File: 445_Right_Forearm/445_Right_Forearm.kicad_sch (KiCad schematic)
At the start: 2 parts, among them J1 69167-107HLF, U1 LSM6DSMTR

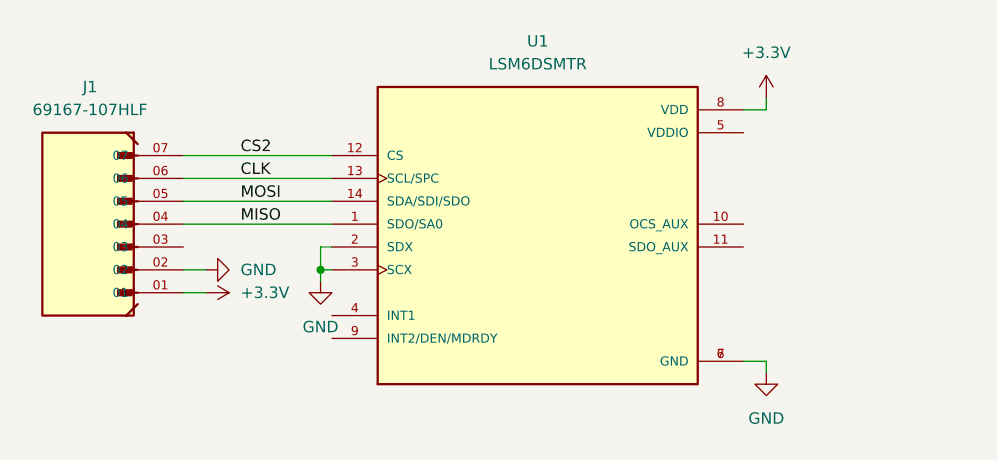
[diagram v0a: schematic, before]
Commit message: enable signal and analog switches
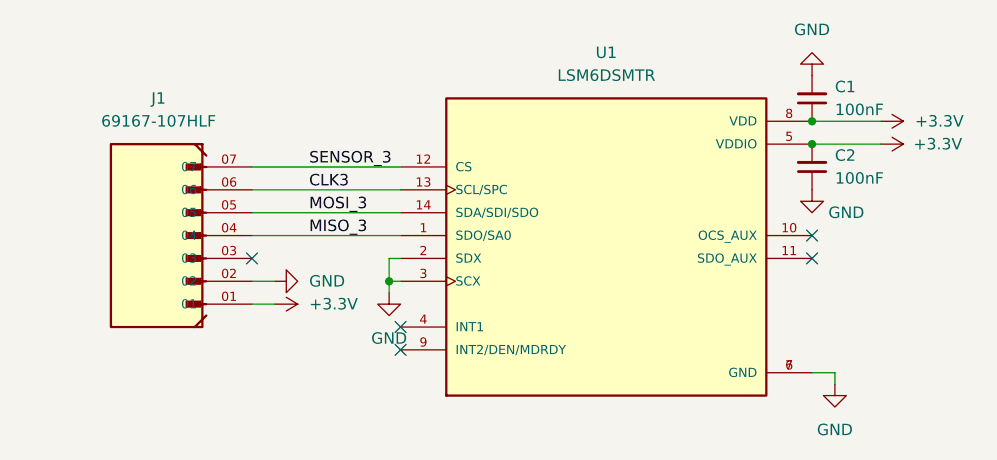
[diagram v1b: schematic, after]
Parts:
- added C1, C2: 100nF, symbol Device:C_Small
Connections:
- net +3.3V: now also U1.5 (VDDIO), C1.1, C2.2
- net GND: now also C1.2, C2.1
- net CLK renamed CLK3
- net CS2 renamed SENSOR_3
- net MISO renamed MISO_3
- net MOSI renamed MOSI_3
- no-connect marks 0 -> 5

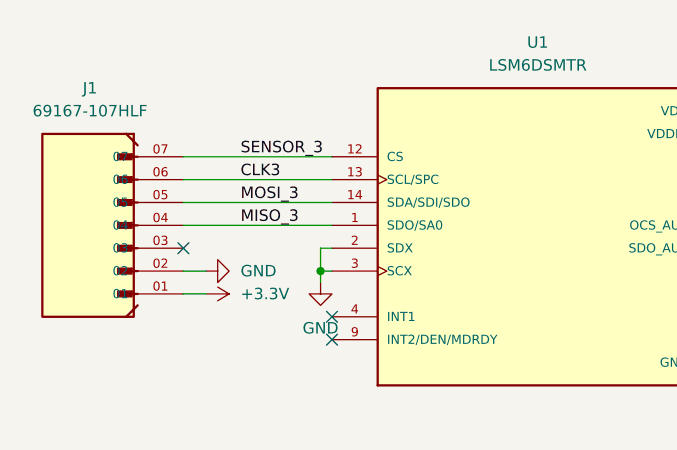
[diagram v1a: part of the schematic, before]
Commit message: replace bicep connector and add int1 connections
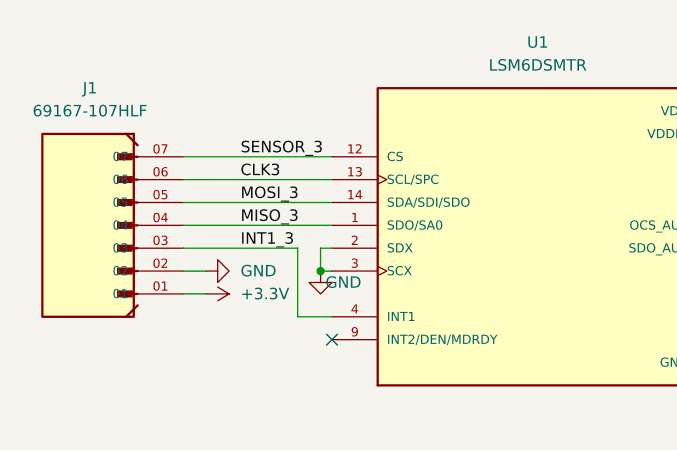
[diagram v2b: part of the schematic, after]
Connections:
- net INT1_3: now reaches J1.03
- net INT1_3: now also U1.4 (INT1)
- no-connect marks 5 -> 3
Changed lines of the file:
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@@
   (junction (at 191.77 77.47) (diameter 0) (color 0 0 0 0)
   )
-  (no_connect (at 146.05 100.33))
   (no_connect (at 191.77 92.71))
-  (no_connect (at 129.54 92.71))
   (no_connect (at 191.77 90.17))
   (no_connect (at 146.05 102.87))
   (wire (pts (xy 191.77 105.41) (xy 194.31 105.41))
-    (stroke (width 0) (type default))
-  )
-  (wire (pts (xy 144.78 95.25) (xy 144.78 92.71))
     (stroke (width 0) (type default))
   )
@@
     (stroke (width 0) (type default))
   )
+  (wire (pts (xy 142.24 92.71) (xy 142.24 100.33))
+    (stroke (width 0) (type default))
+  )
   (wire (pts (xy 194.31 105.41) (xy 194.31 106.68))
     (stroke (width 0) (type default))
@@
     (stroke (width 0) (type default))
   )
-  (wire (pts (xy 144.78 95.25) (xy 146.05 95.25))
+  (wire (pts (xy 129.54 92.71) (xy 142.24 92.71))
     (stroke (width 0) (type default))
   )
-  (wire (pts (xy 144.78 96.52) (xy 144.78 95.25))
+  (wire (pts (xy 144.78 95.25) (xy 146.05 95.25))
     (stroke (width 0) (type default))
   )
@@
     (stroke (width 0) (type default))
   )
+  (wire (pts (xy 144.78 92.71) (xy 144.78 95.25))
+    (stroke (width 0) (type default))
+  )
   (wire (pts (xy 129.54 97.79) (xy 132.08 97.79))
+    (stroke (width 0) (type default))
+  )
+  (wire (pts (xy 142.24 100.33) (xy 146.05 100.33))
     (stroke (width 0) (type default))
   )
@@
   )
   (label "SENSOR_3" (at 135.89 82.55 0) (fields_autoplaced)
+    (effects (font (size 1.27 1.27)) (justify left bottom))
+  )
+  (label "INT1_3" (at 135.89 92.71 0) (fields_autoplaced)
     (effects (font (size 1.27 1.27)) (justify left bottom))
   )
@@
     )
   )
-  (symbol (lib_id "power:GND") (at 144.78 96.52 0) (unit 1)
-    (in_bom yes) (on_board yes) (dnp no) (fields_autoplaced)
-    (property "Reference" "#PWR03" (at 144.78 102.87 0)
+  (symbol (lib_id "power:GND") (at 144.78 95.25 0) (unit 1)
+    (in_bom yes) (on_board yes) (dnp no)
+    (property "Reference" "#PWR03" (at 144.78 101.6 0)
       (effects (font (size 1.27 1.27)) hide)
     )
-    (property "Value" "GND" (at 144.78 101.6 0)
+    (property "Value" "GND" (at 147.32 96.52 0)
       (effects (font (size 1.27 1.27)))
     )
-    (property "Footprint" "" (at 144.78 96.52 0)
+    (property "Footprint" "" (at 144.78 95.25 0)
       (effects (font (size 1.27 1.27)) hide)
     )
-    (property "Datasheet" "" (at 144.78 96.52 0)
+    (property "Datasheet" "" (at 144.78 95.25 0)
       (effects (font (size 1.27 1.27)) hide)
     )

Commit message: Layout First Draft
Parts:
- added H1, H2, H3, H4: MountingHole, MountingHole:MountingHole_2mm, symbol Mechanical:MountingHole
- C1, C2: footprint (none) -> CL21F104ZAANNNC:CAPC2012X135N
- renumbered J1 to J7, U1 to U8
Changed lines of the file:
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@@
     (effects (font (size 1.27 1.27)) (justify left bottom))
+  )
+  (symbol (lib_id "Mechanical:MountingHole") (at 25.4 20.32 0) (unit 1)
+    (in_bom yes) (on_board yes) (dnp no) (fields_autoplaced)
+    (property "Reference" "H1" (at 27.94 19.05 0)
+      (effects (font (size 1.27 1.27)) (justify left))
+    )
+    (property "Value" "MountingHole" (at 27.94 21.59 0)
+      (effects (font (size 1.27 1.27)) (justify left))
+    )
+    (property "Footprint" "MountingHole:MountingHole_2mm" (at 25.4 20.32 0)
+      (effects (font (size 1.27 1.27)) hide)
+    )
+    (property "Datasheet" "~" (at 25.4 20.32 0)
+      (effects (font (size 1.27 1.27)) hide)
+    )
+    (instances
+      (project "445_Right_Forearm"
+        (path "/6bc04bea-814c-4bc3-8d6d-db11891cde88"
+          (reference "H1") (unit 1)
+        )
+      )
+    )
   )
   (symbol (lib_id "power:GND") (at 132.08 95.25 90) (unit 1)
@@
       (effects (font (size 1.27 1.27)) (justify right))
     )
-    (property "Footprint" "" (at 191.77 82.55 0)
+    (property "Footprint" "CL21F104ZAANNNC:CAPC2012X135N" (at 191.77 82.55 0)
       (effects (font (size 1.27 1.27)) hide)
     )
@@
   (symbol (lib_id "69167-107HLF:69167-107HLF") (at 119.38 90.17 180) (unit 1)
     (in_bom yes) (on_board yes) (dnp no) (fields_autoplaced)
-    (property "Reference" "J1" (at 119.1635 74.93 0)
+    (property "Reference" "J7" (at 119.1635 74.93 0)
       (effects (font (size 1.27 1.27)))
     )
@@
       (project "445_Right_Forearm"
         (path "/6bc04bea-814c-4bc3-8d6d-db11891cde88"
-          (reference "J1") (unit 1)
+          (reference "J7") (unit 1)
+        )
+      )
+    )
+  )
+  (symbol (lib_id "Mechanical:MountingHole") (at 25.4 46.99 0) (unit 1)
+    (in_bom yes) (on_board yes) (dnp no) (fields_autoplaced)
+    (property "Reference" "H4" (at 27.94 45.72 0)
+      (effects (font (size 1.27 1.27)) (justify left))
+    )
+    (property "Value" "MountingHole" (at 27.94 48.26 0)
+      (effects (font (size 1.27 1.27)) (justify left))
+    )
+    (property "Footprint" "MountingHole:MountingHole_2mm" (at 25.4 46.99 0)
+      (effects (font (size 1.27 1.27)) hide)
+    )
+    (property "Datasheet" "~" (at 25.4 46.99 0)
+      (effects (font (size 1.27 1.27)) hide)
+    )
+    (instances
+      (project "445_Right_Forearm"
+        (path "/6bc04bea-814c-4bc3-8d6d-db11891cde88"
+          (reference "H4") (unit 1)
         )
       )
@@
     )
   )
+  (symbol (lib_id "Mechanical:MountingHole") (at 25.4 38.1 0) (unit 1)
+    (in_bom yes) (on_board yes) (dnp no) (fields_autoplaced)
+    (property "Reference" "H3" (at 27.94 36.83 0)
+      (effects (font (size 1.27 1.27)) (justify left))
+    )
+    (property "Value" "MountingHole" (at 27.94 39.37 0)
+      (effects (font (size 1.27 1.27)) (justify left))
+    )
+    (property "Footprint" "MountingHole:MountingHole_2mm" (at 25.4 38.1 0)
+      (effects (font (size 1.27 1.27)) hide)
+    )
+    (property "Datasheet" "~" (at 25.4 38.1 0)
+      (effects (font (size 1.27 1.27)) hide)
+    )
+    (instances
+      (project "445_Right_Forearm"
+        (path "/6bc04bea-814c-4bc3-8d6d-db11891cde88"
+          (reference "H3") (unit 1)
+        )
+      )
+    )
+  )
   (symbol (lib_id "Device:C_Small") (at 191.77 74.93 180) (unit 1)
     (in_bom yes) (on_board yes) (dnp no) (fields_autoplaced)
@@
       (effects (font (size 1.27 1.27)) (justify right))
     )
-    (property "Footprint" "" (at 191.77 74.93 0)
+    (property "Footprint" "CL21F104ZAANNNC:CAPC2012X135N" (at 191.77 74.93 0)
       (effects (font (size 1.27 1.27)) hide)
     )
@@
   (symbol (lib_id "LSM6DSMTR:LSM6DSMTR") (at 168.91 90.17 0) (unit 1)
     (in_bom yes) (on_board yes) (dnp no) (fields_autoplaced)
-    (property "Reference" "U1" (at 168.91 69.85 0)
+    (property "Reference" "U8" (at 168.91 69.85 0)
       (effects (font (size 1.27 1.27)))
     )
@@
       (project "445_Right_Forearm"
         (path "/6bc04bea-814c-4bc3-8d6d-db11891cde88"
-          (reference "U1") (unit 1)
-        )
-      )
+          (reference "U8") (unit 1)
+        )
+      )
+    )
+  )
+  (symbol (lib_id "Mechanical:MountingHole") (at 25.4 29.21 0) (unit 1)
+    (in_bom yes) (on_board yes) (dnp no) (fields_autoplaced)
+    (property "Reference" "H2" (at 27.94 27.94 0)
+      (effects (font (size 1.27 1.27)) (justify left))
+    )
+    (property "Value" "MountingHole" (at 27.94 30.48 0)
+      (effects (font (size 1.27 1.27)) (justify left))
+    )
+    (property "Footprint" "MountingHole:MountingHole_2mm" (at 25.4 29.21 0)
+      (effects (font (size 1.27 1.27)) hide)
+    )
+    (property "Datasheet" "~" (at 25.4 29.21 0)
+      (effects (font (size 1.27 1.27)) hide)
+    )
+    (instances
+      (project "445_Right_Forearm"
+        (path "/6bc04bea-814c-4bc3-8d6d-db11891cde88"
+          (reference "H2") (unit 1)
+        )
+      )
